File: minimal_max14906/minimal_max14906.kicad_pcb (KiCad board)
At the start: 4 copper layers, 55.9 x 34.9 mm, 72 parts, among them J1 CLP-114-02-G-D-BE, J2 CLP-102-02-G-D-BE, J3 CLP-102-02-G-D-BE, J4 CLP-104-02-G-D-BE, J5 CLP-104-02-G-D-BE, J6 CLP-102-02-G-D-BE, J7 CLP-102-02-G-D-BE, Q1 SI7309DN-T1-E3, Q2 SI7309DN-T1-E3, Q3 SI7309DN-T1-E3, Q4 SI7309DN-T1-E3, U1 MAX14906ATM+

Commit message: Update KiCAD Symbol Generator and configuration files
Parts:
- removed REF** (x6): mouse-bite-midle-50mil-200mil, mouse_bite_footprints:mouse-bite-midle-50mil-200mil
- removed REF**: mouse-bite-50mil-790mil, mouse_bite_footprints:mouse-bite-50mil-790mil
- added MB1: mouse-bite-midle-50mil-200mil, mouse_bite_footprints:mouse-bite-midle-50mil-200mil, F.Cu at (153.7, 94.5)
- added MB2: mouse-bite-midle-50mil-200mil, mouse_bite_footprints:mouse-bite-midle-50mil-200mil, F.Cu at (153.7, 104.7)
- added MB3: mouse-bite-midle-50mil-200mil, mouse_bite_footprints:mouse-bite-midle-50mil-200mil, F.Cu at (116.8, 94.5)
- added MB4: mouse-bite-midle-50mil-200mil, mouse_bite_footprints:mouse-bite-midle-50mil-200mil, F.Cu at (153.7, 112.3)
- added MB5: mouse-bite-midle-50mil-200mil, mouse_bite_footprints:mouse-bite-50mil-790mil, F.Cu at (135.3, 89.6)
- added MB6: mouse-bite-midle-50mil-200mil, mouse_bite_footprints:mouse-bite-midle-50mil-200mil, F.Cu at (116.8, 104.7)
- added MB7: mouse-bite-midle-50mil-200mil, mouse_bite_footprints:mouse-bite-midle-50mil-200mil, F.Cu at (116.8, 112.3)

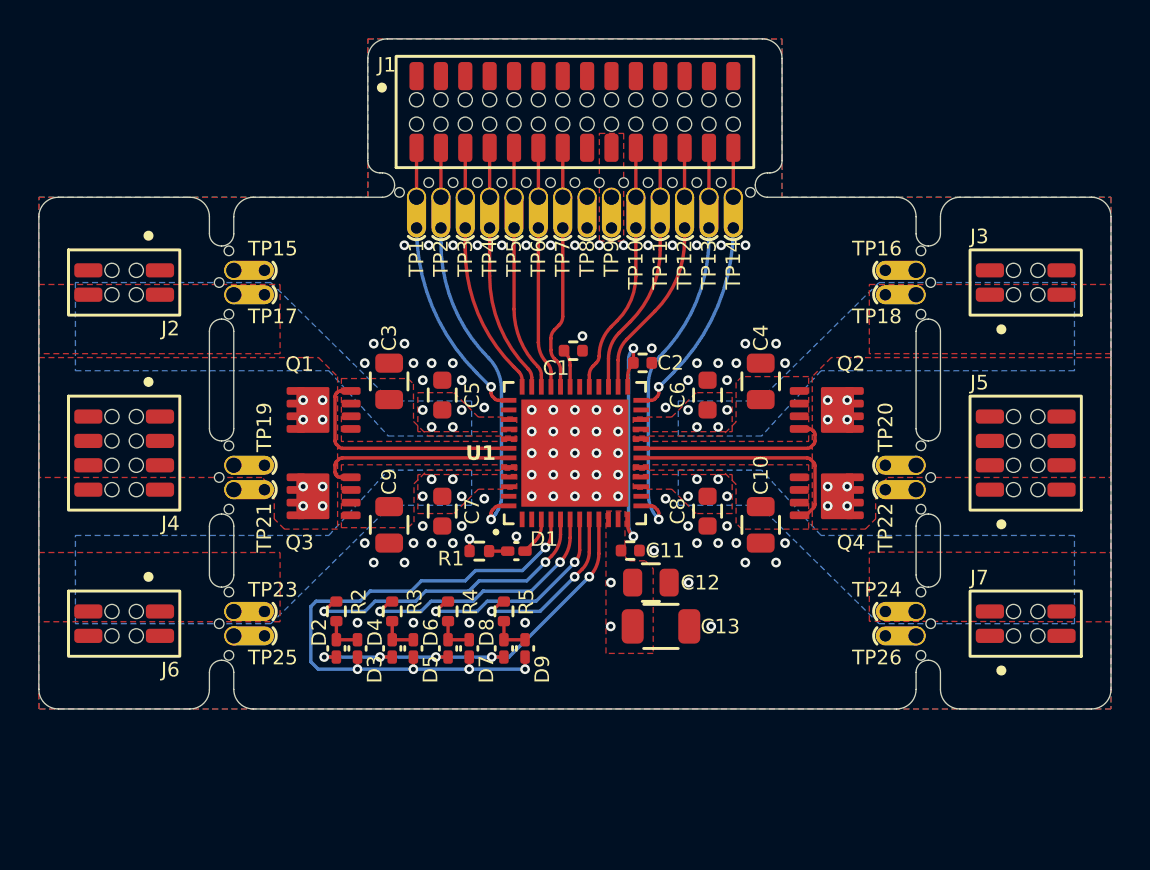
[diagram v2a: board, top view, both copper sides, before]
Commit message: Update KiCAD Symbol Generator subproject and add new footprints for fiducial markers
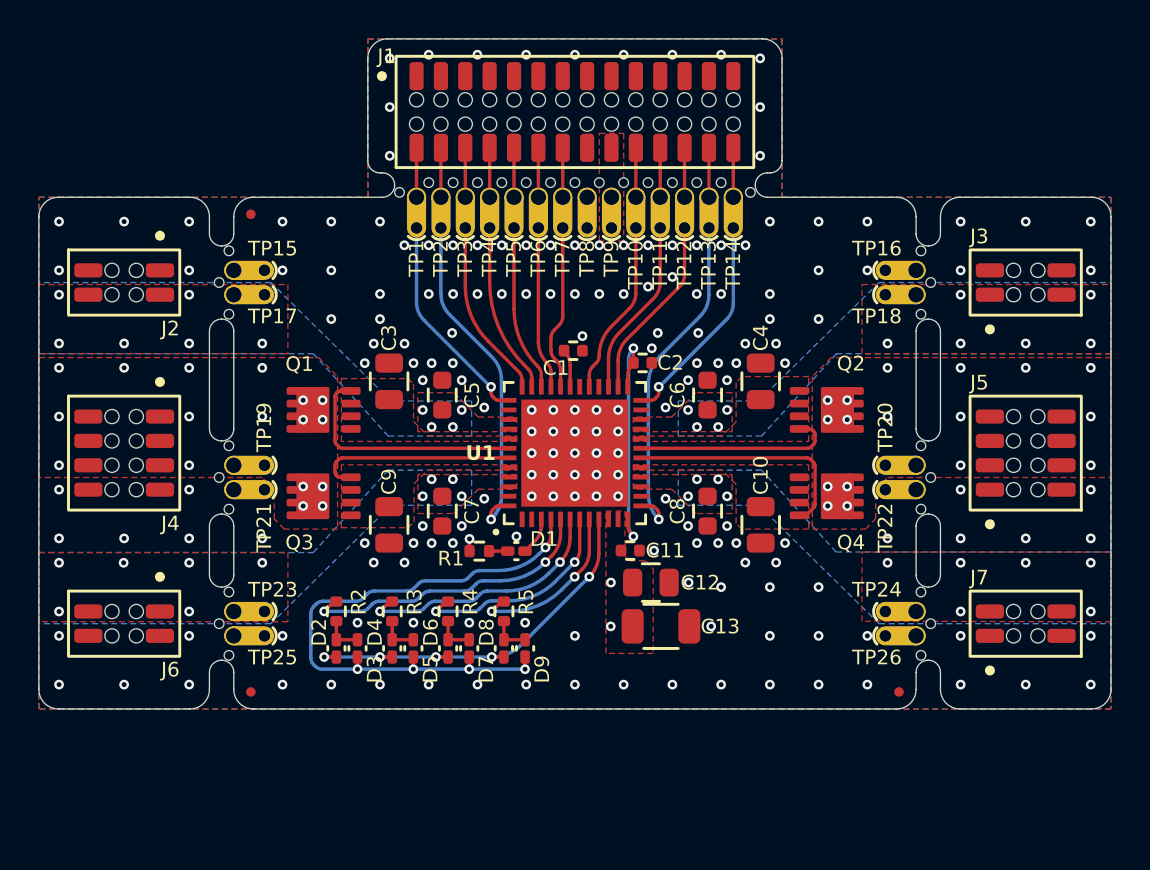
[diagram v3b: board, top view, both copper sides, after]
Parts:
- added FID1: Fiducial, no_components_footprints:Fiducial_0.5mm_Mask1mm, F.Cu at (118.4, 91.0)
- added FID2: Fiducial, no_components_footprints:Fiducial_0.5mm_Mask1mm, F.Cu at (118.4, 115.9)
- added FID3: Fiducial, no_components_footprints:Fiducial_0.5mm_Mask1mm, F.Cu at (152.1, 115.9)
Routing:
- net GNDA: vias 86 -> 184
- net /VDD_24V_MAX14906: vias 19 -> 37
- net /CHANNEL_4: vias 4 -> 10
- net /CHANNEL_3: vias 4 -> 10
- net /CHANNEL_2: vias 4 -> 10
- net /CHANNEL_1: vias 4 -> 10

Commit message: Update KiCAD Symbol Generator with new features and improvements
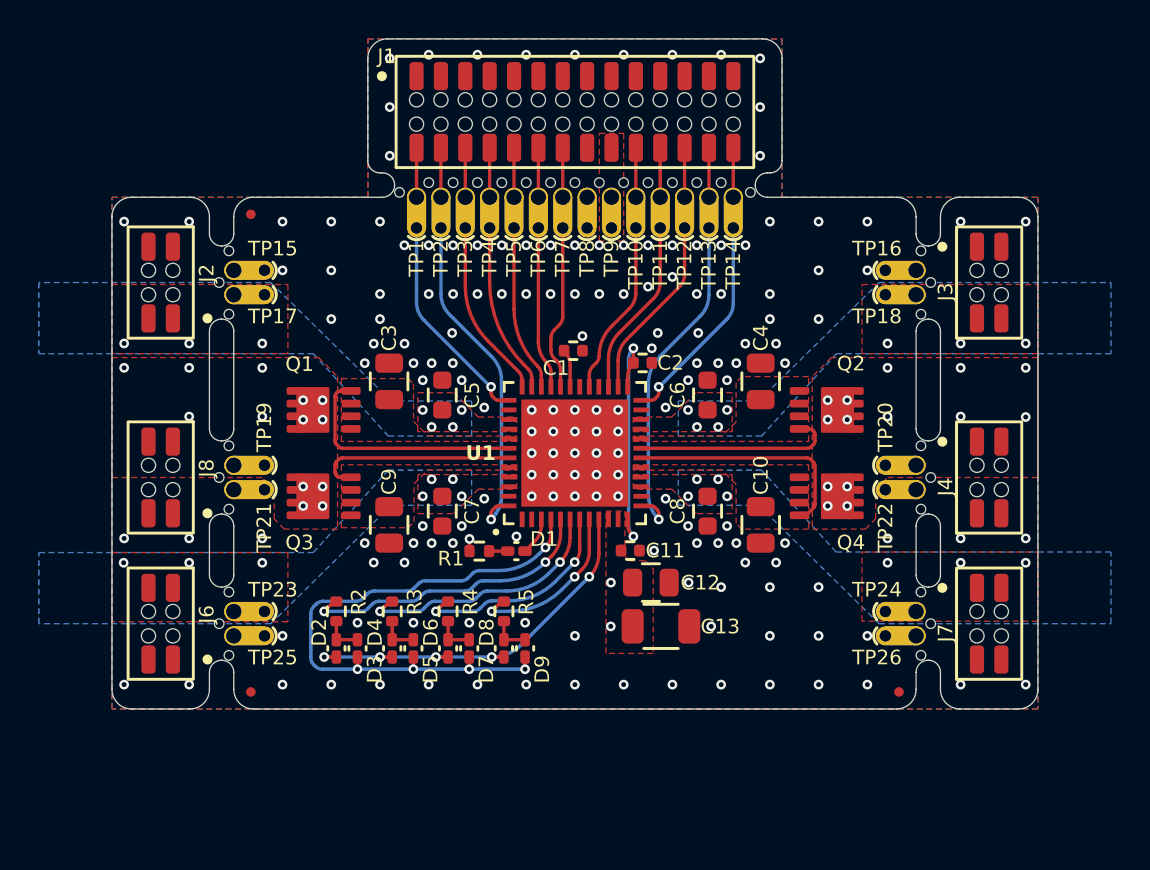
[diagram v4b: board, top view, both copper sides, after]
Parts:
- removed J5: CLP-104-02-G-D-BE, connector_footprints:CLP-104-02-G-D-BE
- added J8: CLP-102-02-G-D-BE, connector_footprints:CLP-102-02-G-D-BE, F.Cu at (113.7, 104.7)
- J4: value CLP-104-02-G-D-BE -> CLP-102-02-G-D-BE; footprint connector_footprints:CLP-104-02-G-D-BE -> connector_footprints:CLP-102-02-G-D-BE
- moved J4 45.1 mm to (156.8, 104.7), turned to 0 degrees
- moved J2 1.91 mm to (113.7, 94.5), turned to 180 degrees
- moved J3 1.91 mm to (156.8, 94.5), turned to 0 degrees
- moved J6 1.91 mm to (113.7, 112.3), turned to 180 degrees
- moved J7 1.91 mm to (156.8, 112.3), turned to 0 degrees
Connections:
- J2 pad 1: GNDA -> /CHANNEL_3
- J2 pad 4: /CHANNEL_3 -> GNDA
- J3 pad 1: /CHANNEL_2 -> GNDA
- J3 pad 4: GNDA -> /CHANNEL_2
- J4 pad 1: unconnected-(J4-Pad1) -> /VDD_24V_MAX14906
- J4 pad 2: unconnected-(J4-Pad2) -> GNDA
- J4 pad 3: unconnected-(J4-Pad3) -> /VDD_24V_MAX14906
- J4 pad 4: unconnected-(J4-Pad4) -> GNDA
- J6 pad 1: /CHANNEL_4 -> GNDA
- J6 pad 4: GNDA -> /CHANNEL_4
- J7 pad 1: GNDA -> /CHANNEL_1
- J7 pad 4: /CHANNEL_1 -> GNDA
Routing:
- net GNDA: vias 184 -> 166
- net /VDD_24V_MAX14906: vias 37 -> 30
- net /CHANNEL_4: vias 10 -> 7
- net /CHANNEL_3: vias 10 -> 7
- net /CHANNEL_2: vias 10 -> 7
- net /CHANNEL_1: vias 10 -> 7
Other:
- board size 55.9 x 34.9 mm -> 48.3 x 34.9 mm

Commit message: Update KiCAD Symbol Generator with enhancements and bug fixes
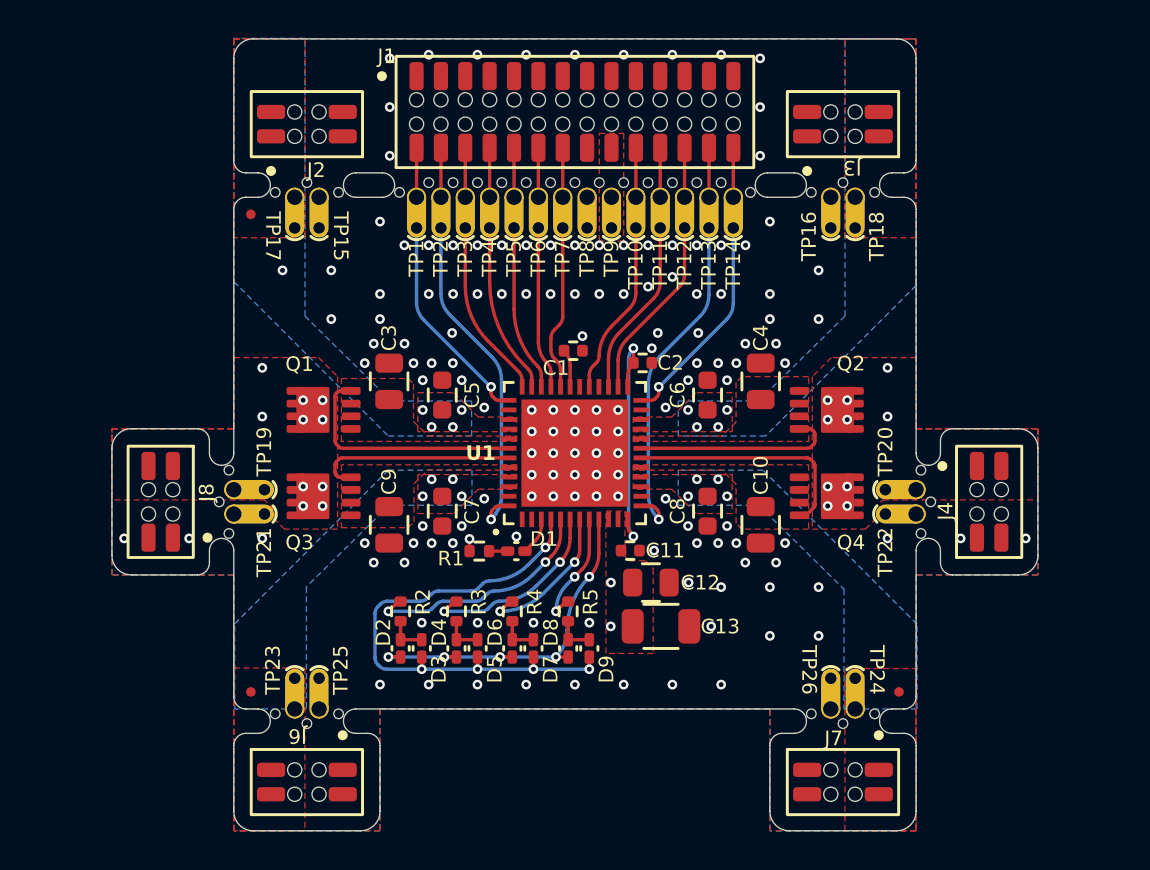
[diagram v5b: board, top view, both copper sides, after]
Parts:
- moved J6 11.2 mm to (121.3, 120.6), turned to -90 degrees
- moved J2 11.2 mm to (121.3, 86.3), turned to 90 degrees
- moved J7 11.2 mm to (149.2, 120.6), turned to -90 degrees
- moved J3 11.2 mm to (149.2, 86.3), turned to 90 degrees
- moved MB1 6.75 mm to (149.2, 89.5), turned to 0 degrees
- moved MB3 6.75 mm to (121.3, 89.5), turned to 0 degrees
- moved MB4 6.75 mm to (149.2, 117.4), turned to 180 degrees
- moved MB7 6.75 mm to (121.3, 117.4), turned to 180 degrees
- moved TP17 5.99 mm to (120.7, 90.1), turned to -90 degrees
- moved TP18 5.99 mm to (149.9, 90.1), turned to -90 degrees
- moved TP23 5.99 mm to (120.7, 116.8), turned to 90 degrees
- moved TP24 5.99 mm to (149.9, 116.8), turned to 90 degrees
- moved TP15 5.85 mm to (121.9, 90.1), turned to -90 degrees
- moved TP16 5.85 mm to (148.6, 90.1), turned to -90 degrees
- moved TP25 5.85 mm to (121.9, 116.8), turned to 90 degrees
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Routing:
- net /FLED: track 31.3 -> 28.0 mm
- net /L2: track 11.3 -> 7.96 mm
- net /L3: track 13.4 -> 10.1 mm
- net /L4: track 15.6 -> 12.3 mm
- net /L1: track 8.98 -> 6.20 mm
- net /SLED: track 21.1 -> 19.0 mm
- net GNDA: vias 166 -> 145
- net /VDD_24V_MAX14906: vias 30 -> 23
- net /CHANNEL_4: vias 7 -> 4
- net /CHANNEL_3: vias 7 -> 4
- net /CHANNEL_2: vias 7 -> 4
- net /CHANNEL_1: vias 7 -> 4
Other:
- board size 48.3 x 34.9 mm -> 48.3 x 41.3 mm

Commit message: Update KiCAD schematic references for consistency and accuracy
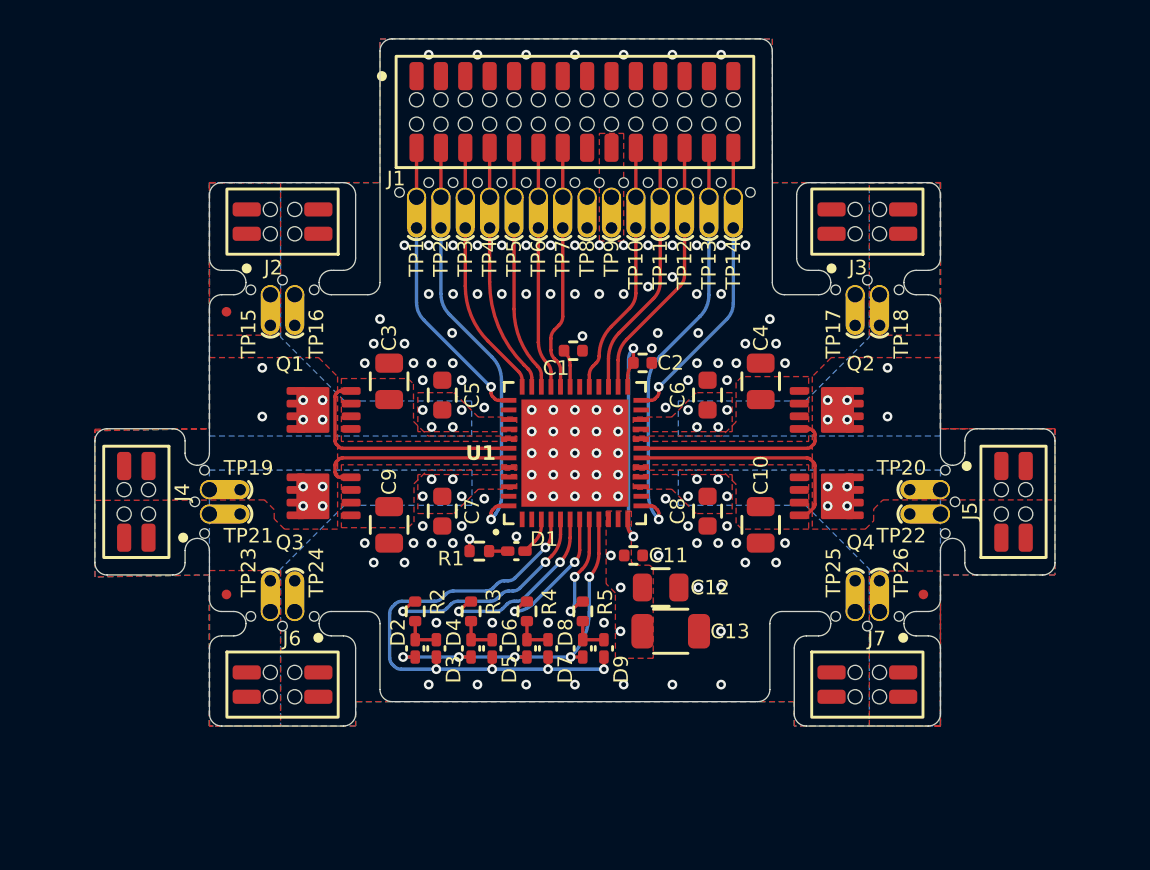
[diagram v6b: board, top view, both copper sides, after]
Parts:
- moved J7 5.24 mm to (150.5, 115.5)
- moved J6 5.24 mm to (120.0, 115.5)
- moved FID1 5.24 mm to (117.1, 96.1)
- moved FID2 5.24 mm to (117.1, 110.8)
- moved FID3 5.24 mm to (153.4, 110.8)
- moved J3 5.24 mm to (150.5, 91.4)
- moved MB3 5.24 mm to (150.5, 94.5)
- moved MB7 5.24 mm to (150.5, 112.3)
- moved TP15 5.24 mm to (119.4, 95.2)
- moved TP17 5.24 mm to (149.9, 95.2)
- moved TP23 5.24 mm to (119.4, 111.7)
- moved TP25 5.24 mm to (149.9, 111.7)
- moved J2 5.24 mm to (120.0, 91.4)
- moved MB2 5.24 mm to (120.0, 94.5)
- moved MB6 5.24 mm to (120.0, 112.3)
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- renumbered J8 to J4, J4 to J5, MB5 to MB1, MB3 to MB2, MB1 to MB3, MB6 to MB4, MB2 to MB5, MB7 to MB6, MB4 to MB7, TP17 to TP15, TP15 to TP16, TP16 to TP17, TP25 to TP24, TP26 to TP25, TP24 to TP26
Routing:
- net /L2: track 7.96 -> 7.29 mm
- net /L3: track 10.1 -> 9.47 mm
- net /FLED: track 28.0 -> 27.4 mm
- net /L4: track 12.3 -> 11.7 mm
- net GNDA: vias 145 -> 119
- net /VDD_24V_MAX14906: vias 23 -> 24
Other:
- board size 48.3 x 41.3 mm -> 50 x 35.8 mm

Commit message: Backup
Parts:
- moved FID1 5.10 mm to (122.2, 96.1)
- moved FID2 5.10 mm to (122.2, 110.8)
- moved FID3 5.10 mm to (148.3, 110.8)
- moved J1 1.27 mm to (135.3, 86.9)
- moved J4 1.27 mm to (113.7, 106.0)
- moved J5 1.27 mm to (156.8, 106.0)
- moved MB4 1.27 mm to (116.8, 106.0)
- moved MB5 1.27 mm to (153.7, 106.0)
- moved TP20 1.27 mm to (153.0, 105.3)
- moved TP22 1.27 mm to (153.0, 106.6)
- moved MB1 1.27 mm to (135.3, 90.9)
- moved TP1 1.27 mm to (127.0, 91.4)
- moved TP10 1.27 mm to (138.4, 91.4)
- moved TP11 1.27 mm to (139.7, 91.4)
- moved TP12 1.27 mm to (141.0, 91.4)
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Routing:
- net /~{READY}: track 14.0 -> 10.9 mm
- net /CLK: track 11.0 -> 9.76 mm
- net /~{FAULT}: track 11.7 -> 10.4 mm
- net /~{CS}: track 11.2 -> 9.94 mm
- net /SYNCH: track 11.9 -> 10.6 mm
- net /SDO: track 11.2 -> 9.93 mm
- net /SDI: track 11.4 -> 10.2 mm
- net /D4: track 20.5 -> 19.2 mm
- net /D3: track 13.8 -> 12.6 mm
- net /D2: track 13.9 -> 12.6 mm
- net /D1: track 20.5 -> 19.2 mm
- net /EN: track 11.8 -> 10.6 mm
- net GNDA: vias 119 -> 104
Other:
- board size 50 x 35.8 mm -> 47.5 x 34.5 mm
